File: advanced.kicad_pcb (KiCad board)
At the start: 2 copper layers, 108 parts, among them U1 ATtiny24-20P, U2 ATtiny28L-4P, U3 ATtiny13A-P, U4 ATtiny25-20P, U5 ATtiny24-20P, U6 ATtiny85-20P

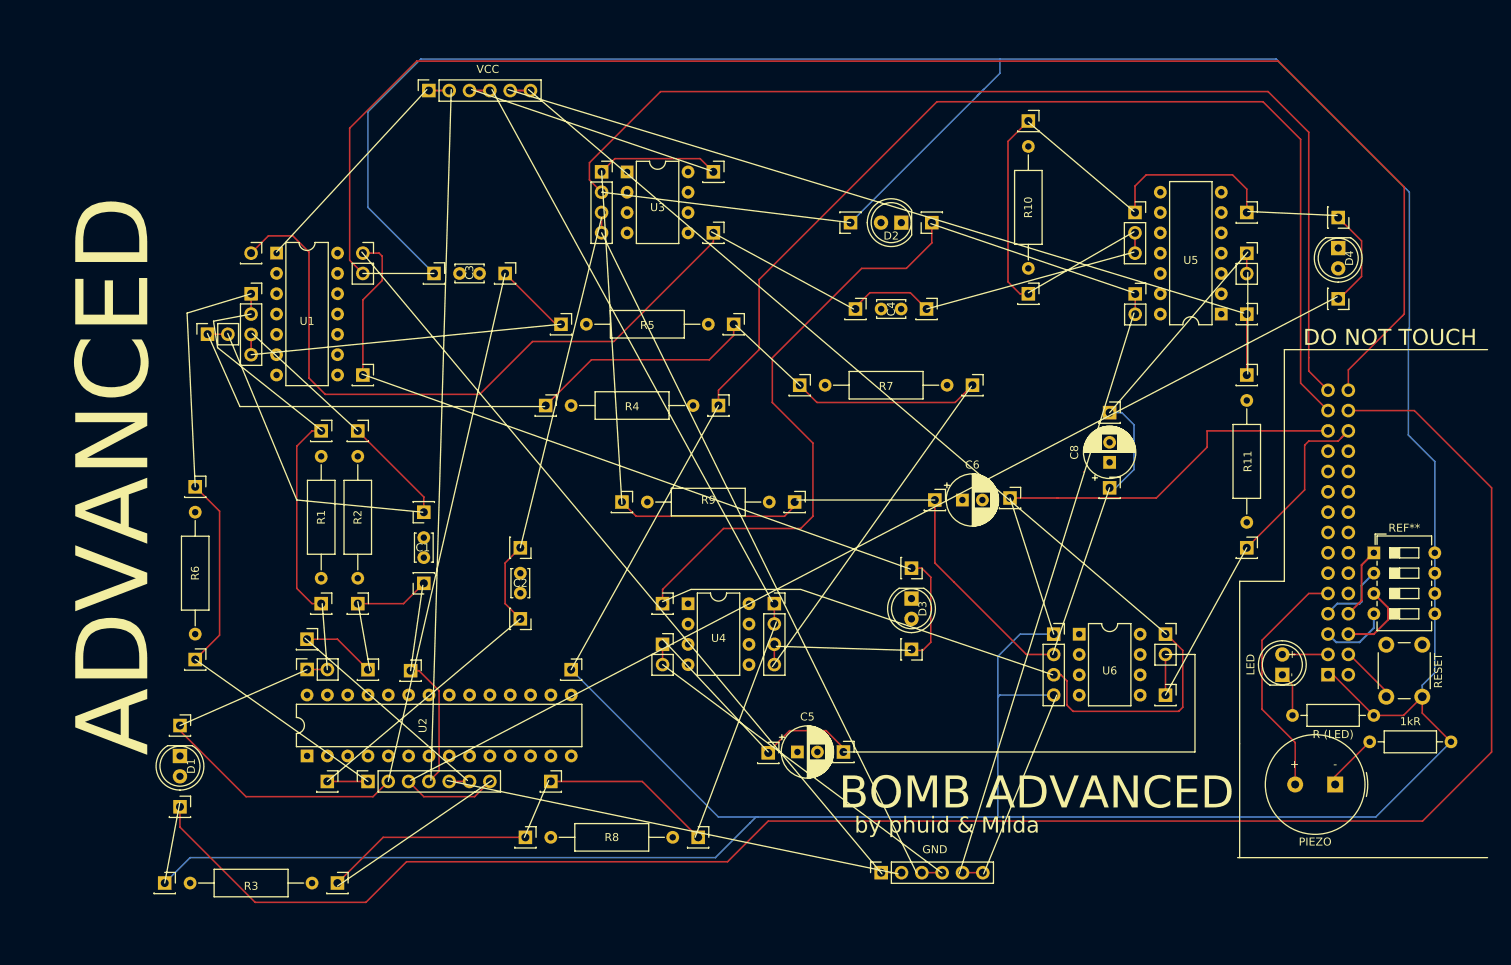
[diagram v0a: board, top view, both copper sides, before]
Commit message: outline added, part list corrected, resistor tag added, continuity check
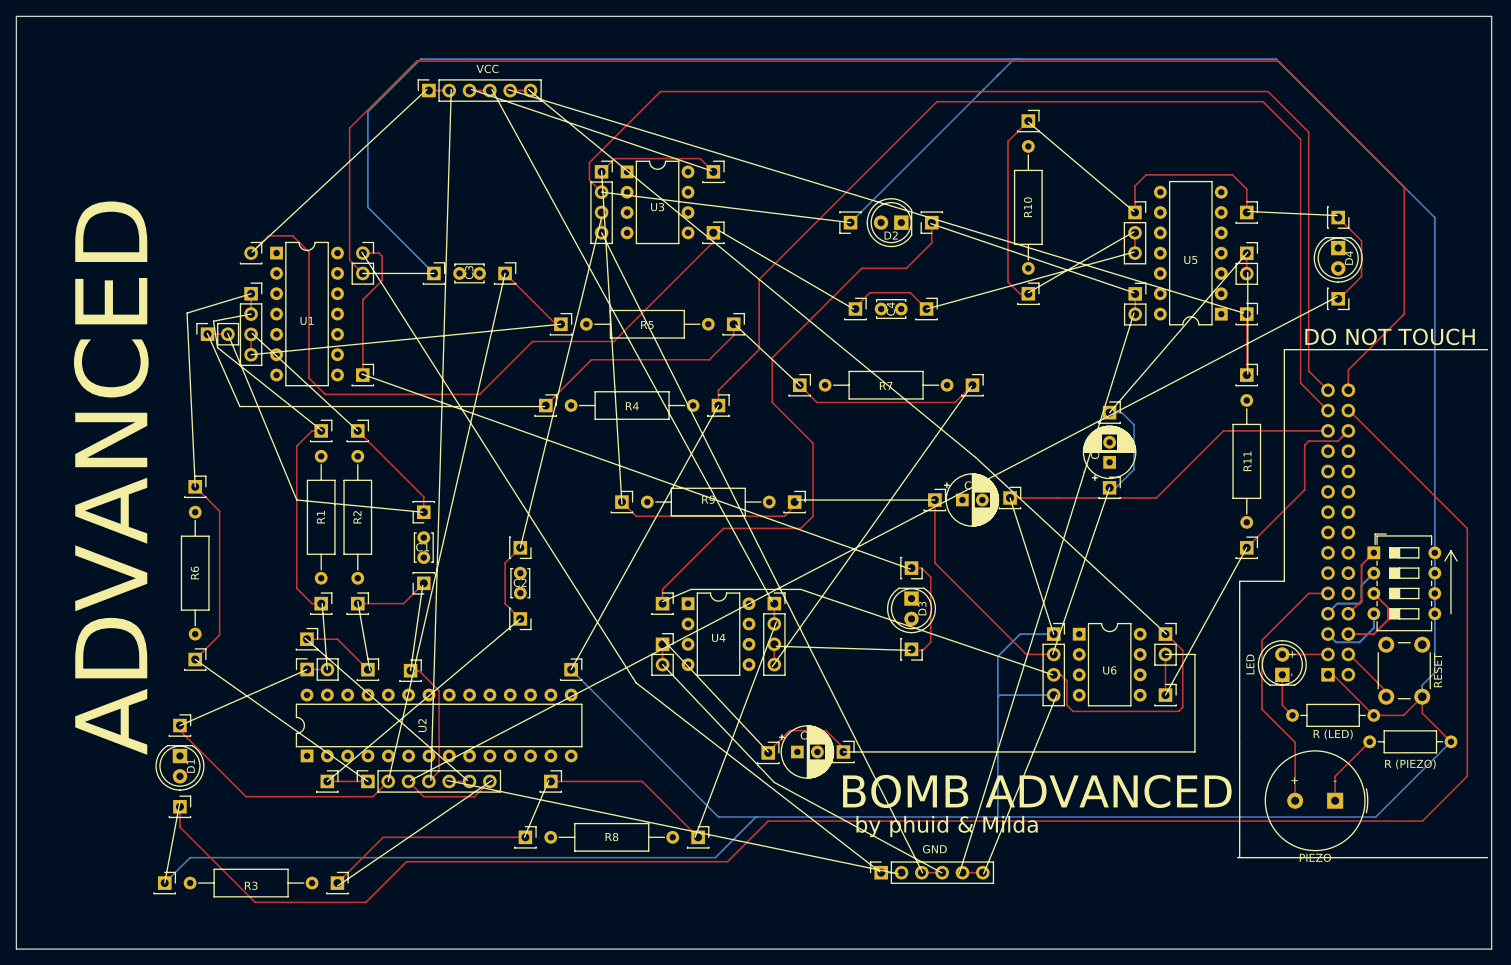
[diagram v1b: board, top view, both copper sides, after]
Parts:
- R (PIEZO): renamed from 1kR
- moved PIEZO 2.03 mm to (246.6, 145.3)
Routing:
- net (no net): track 2063.7 -> 2061.1 mm
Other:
- board outline added: 184.4 x 116.6 mm

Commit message: board shrunk to 10*10 , all pads now round
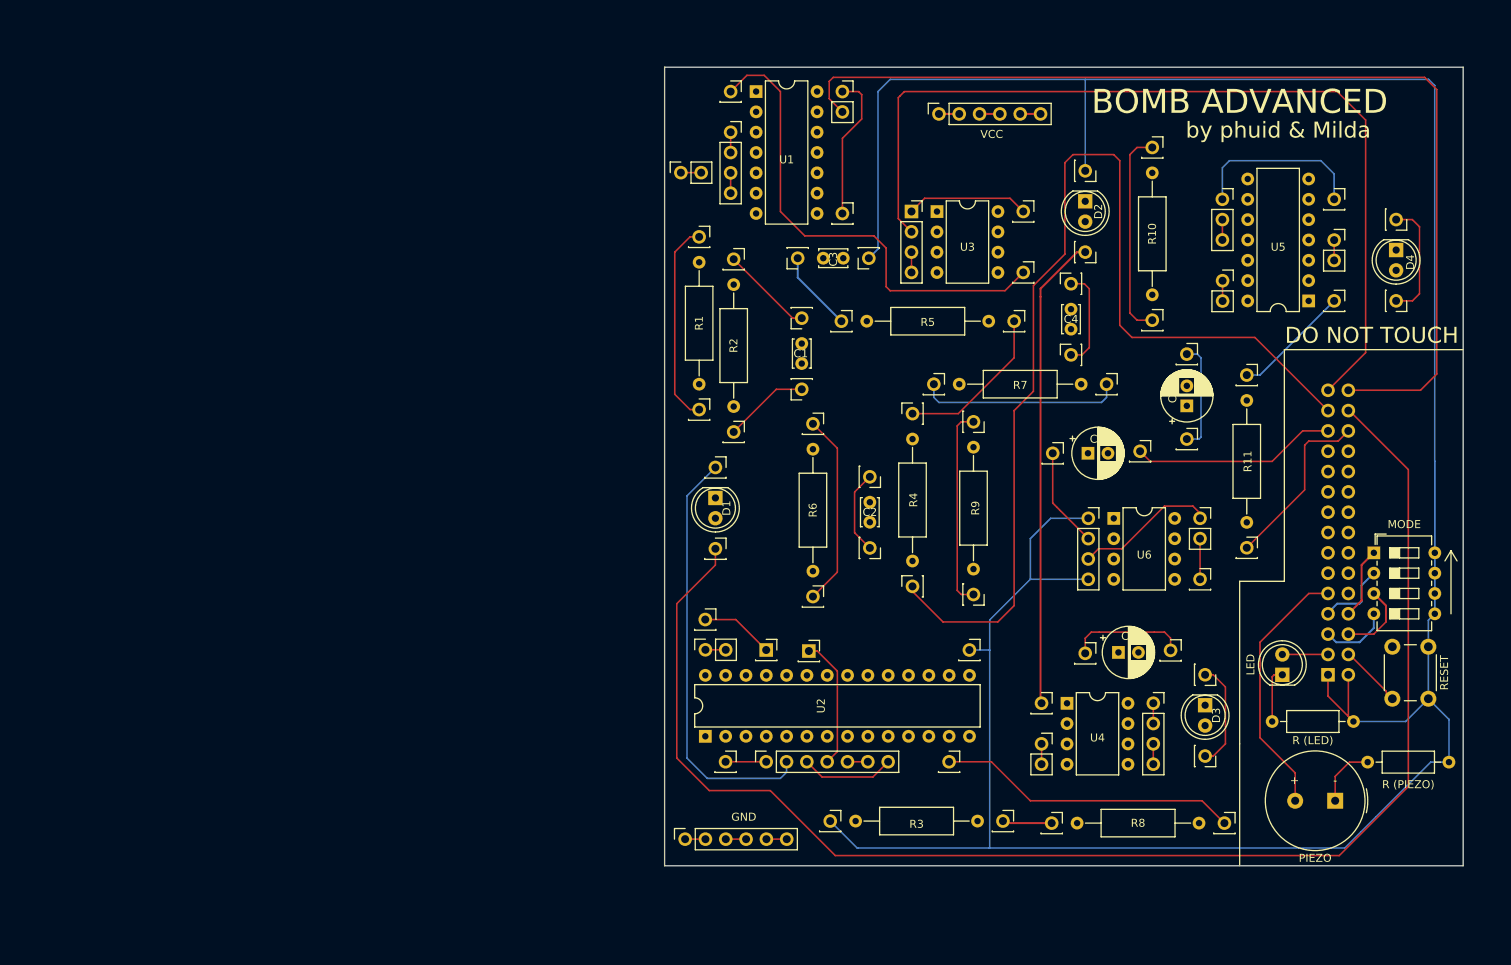
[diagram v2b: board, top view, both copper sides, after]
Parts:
- C1, C2: value C -> 10pF
- C3, C4: value C -> 50mF
- C5, C6, C8: value C_Polarized -> 100mF
- R1, R3, R7, R9: value R -> 100kR
- R10: value 2000 -> 5MR
- R11, R2, R5, R6: value R -> 4.7kR
- R4, R8: value R -> 5MR
- moved R3 83.5 mm to (201.9, 147.8)
- moved   83.5 mm to (205.1, 147.8)
- moved   83.5 mm to (183.5, 147.8)
- moved   77.6 mm to (181.4, 98.2)
- moved   77.6 mm to (181.4, 119.8)
- moved R6 77.6 mm to (181.4, 101.3)
- moved   74.3 mm to (169.2, 103.6)
- moved D1 74.3 mm to (169.2, 107.4)
- moved   74.3 mm to (169.2, 113.8)
- moved   65.8 mm to (211.2, 148.1)
- moved   65.8 mm to (232.8, 148.1)
- moved R8 65.8 mm to (214.4, 148.1)
- moved REF** 63.8 mm to (197.1, 59.4)
- moved   63.3 mm to (185.0, 71.9)
- moved   63.3 mm to (171.1, 56.6)
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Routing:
- net (no net): track 2061.1 -> 1721.8 mm
- net Net-(D4-Pad1): track 8.58 -> 0.00 mm
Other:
- board size 184.4 x 116.6 mm -> 99.8 x 99.8 mm
- board text added: "MODE"
- board text removed: "ADVANCED"
